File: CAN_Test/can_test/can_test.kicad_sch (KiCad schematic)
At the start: 8 parts, among them IC1 TCAN3414DR, IC2 TCAN3414DR, J1 Conn_01x04_Pin, U1 Teensy4.0

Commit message: remove lock files
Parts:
- U1: footprint (none) -> teensy:Teensy40_SMT
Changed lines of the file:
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@@
 			)
 		)
-		(property "Footprint" ""
+		(property "Footprint" "teensy:Teensy40_SMT"
 			(at 50.8 57.15 0)
 			(effects

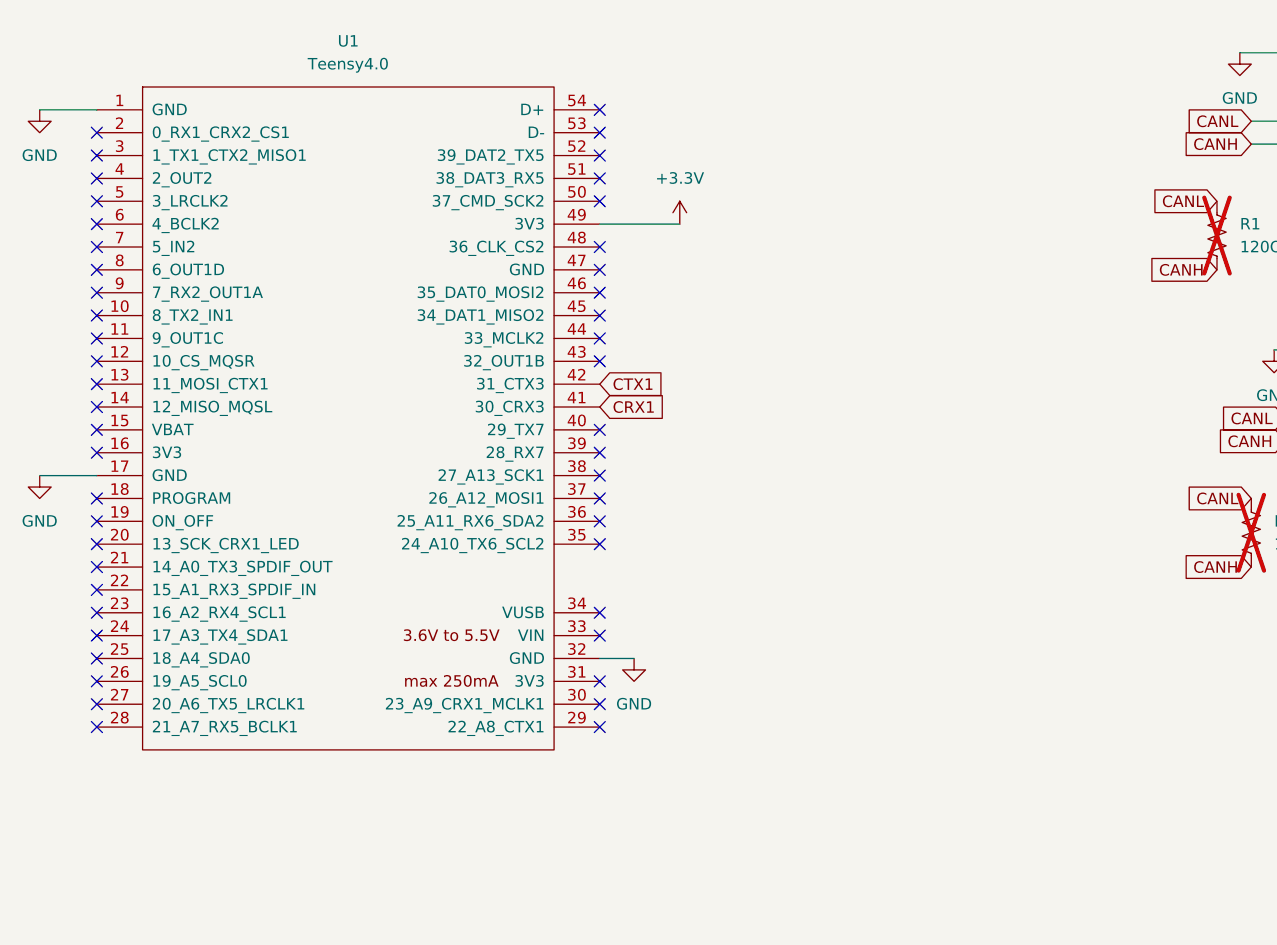
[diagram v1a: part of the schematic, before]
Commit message: update can test to teensy 41
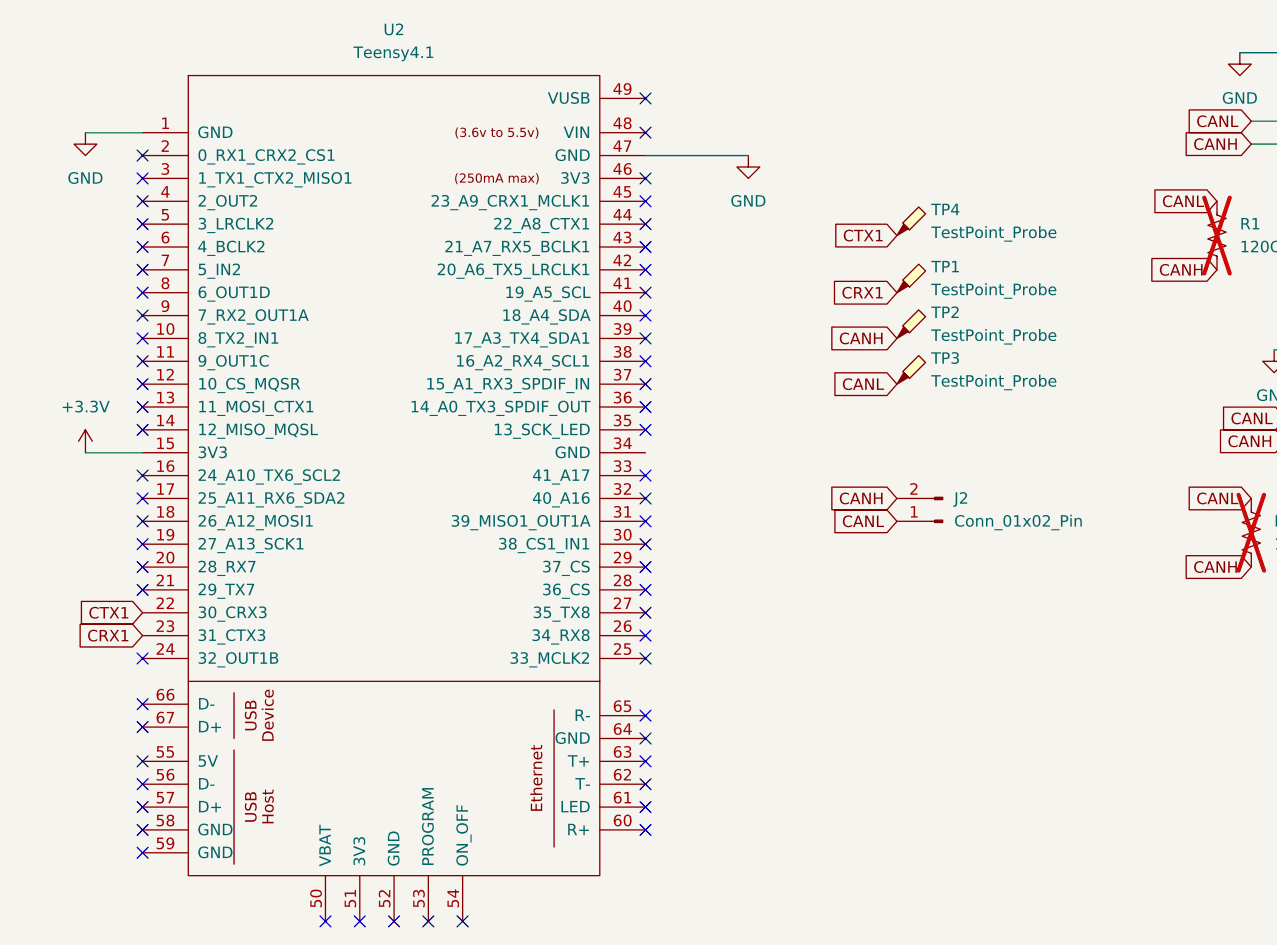
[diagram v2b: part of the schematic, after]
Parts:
- removed U1: Teensy4.0, teensy:Teensy40_SMT, symbol teensy:Teensy4.0
- added J2: Conn_01x02_Pin, Connector_PinHeader_2.54mm:PinHeader_1x02_P2.54mm_Vertical, symbol Connector:Conn_01x02_Pin
- added TP1, TP2, TP3, TP4: TestPoint_Probe, TestPoint:TestPoint_Plated_Hole_D3.0mm, symbol Connector:TestPoint_Probe
- added U2: Teensy4.1, teensy:Teensy41, symbol teensy:Teensy4.1
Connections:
- net +3.3V: now also U2.15 (3V3)
- net CANH: now also J2.2 (Pin_2), TP2.1
- net CANL: now also J2.1 (Pin_1), TP3.1
- net CRX1: now also TP1.1, U2.23 (31_CTX3)
- net CTX1: now also TP4.1, U2.22 (30_CRX3)
- net GND: now also U2.1 (GND), U2.47 (GND)
- no-connect marks 48 -> 61

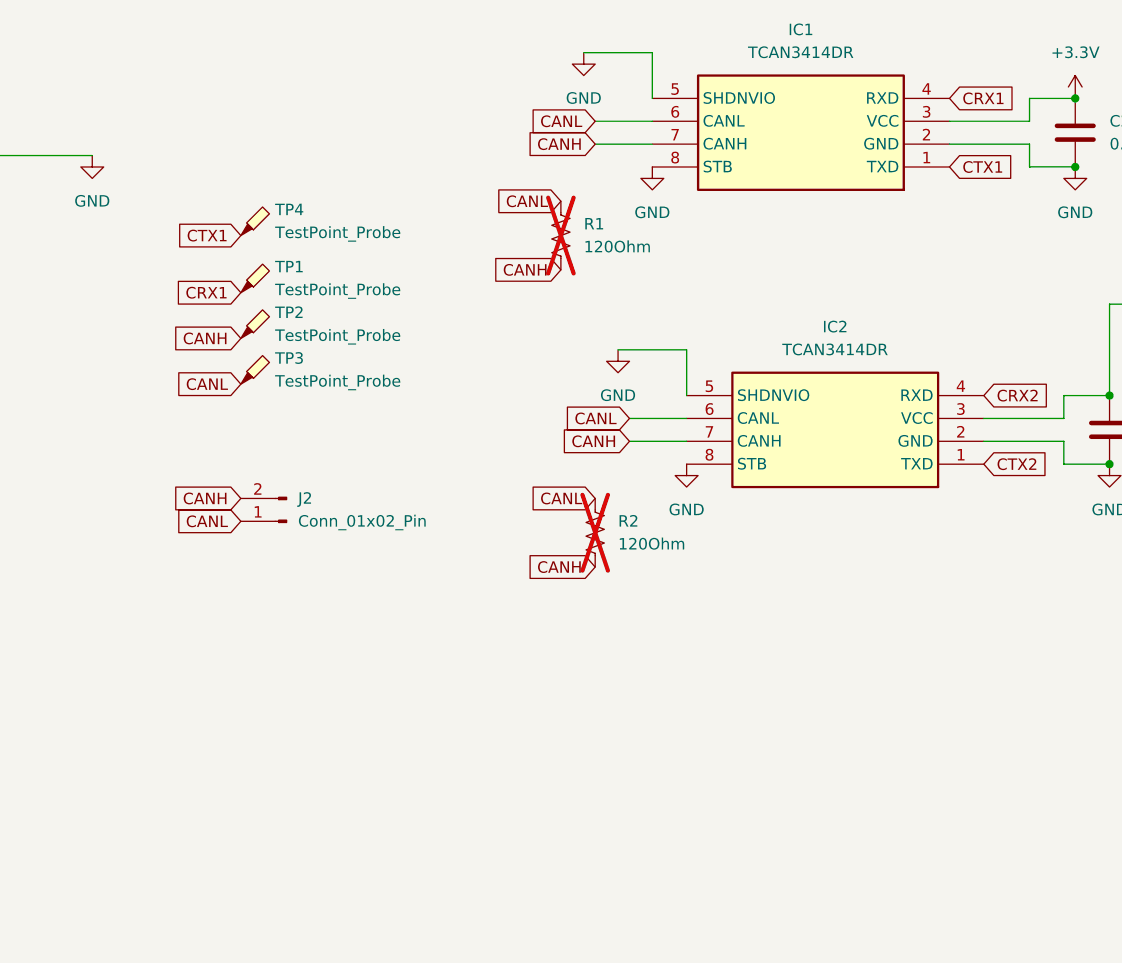
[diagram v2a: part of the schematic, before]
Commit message: make fixes sylvester reccomended
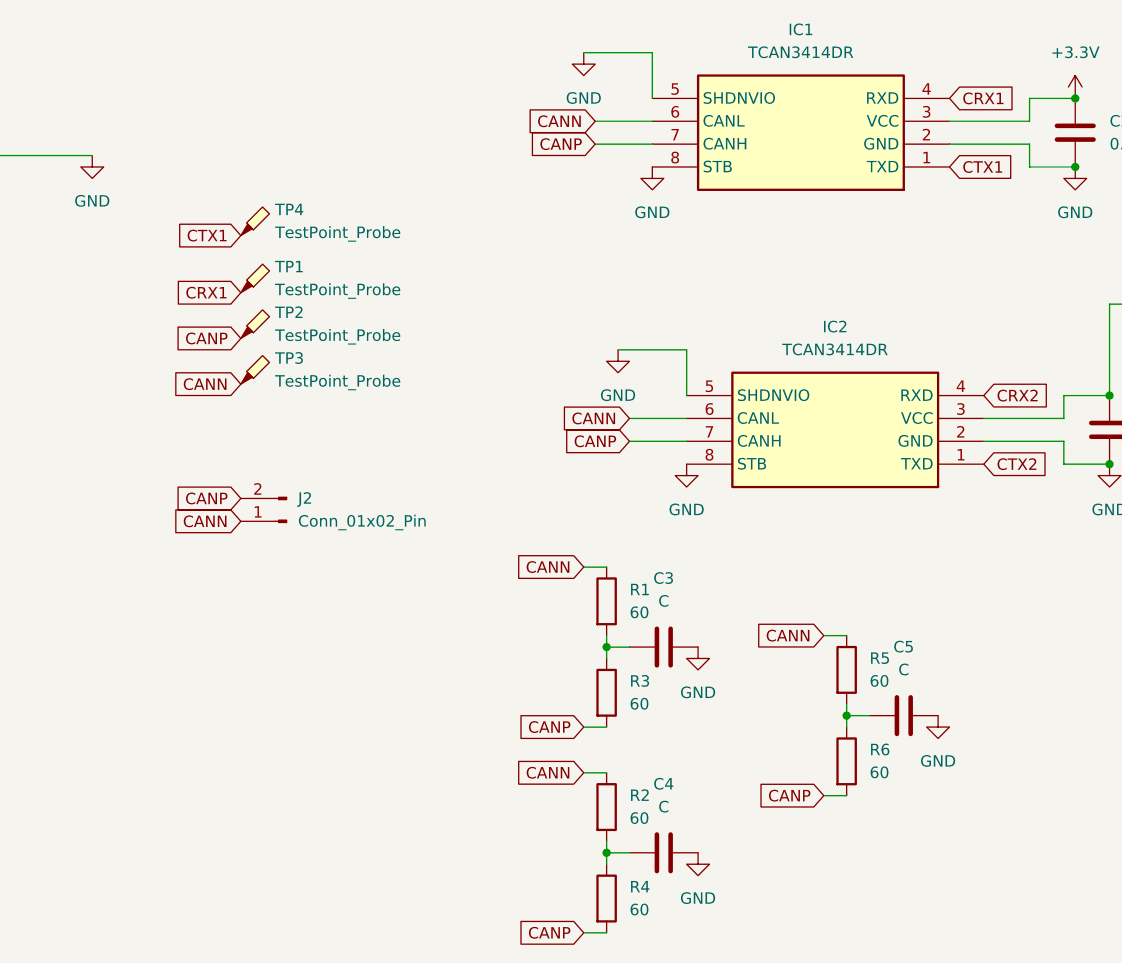
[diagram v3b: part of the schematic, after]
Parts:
- removed R1, R2: 120Ohm, Resistor_SMD:R_0805_2012Metric_Pad1.20x1.40mm_HandSolder, symbol Device:R_US
- added C3, C4, C5: C, Capacitor_SMD:C_0805_2012Metric_Pad1.18x1.45mm_HandSolder, symbol Device:C
- added R1, R2, R3, R4, R5, R6: 60, Resistor_SMD:R_0805_2012Metric_Pad1.20x1.40mm_HandSolder, symbol Device:R
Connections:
- net GND: now also C3.2, C4.2, C5.2
- net CANH renamed CANP
- net CANP: now also R3.2, R4.2, R6.2
- net CANL renamed CANN
- net CANN: now also R1.1, R2.1, R5.1
- new net: C5.1, R5.2, R6.1
- new net: C4.1, R2.2, R4.1
- new net: C3.1, R1.2, R3.1

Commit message: cleanup schematic
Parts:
- removed C5: C, Capacitor_SMD:C_0805_2012Metric_Pad1.18x1.45mm_HandSolder, symbol Device:C
- removed R5, R6: 60, Resistor_SMD:R_0805_2012Metric_Pad1.20x1.40mm_HandSolder, symbol Device:R
- C3, C4, R1, R2, R3, R4: now not fitted
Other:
- note added: "CAN dupont"
- note added: "CAN filter (dont think we need with how short distance)"
- note added: "INPUT -> transiever from jetson"
- note added: "Sanity checking points"
- note added: "Teensy transiever"
- moved on the sheet: C1, C2, IC1, IC2, J1, J2
